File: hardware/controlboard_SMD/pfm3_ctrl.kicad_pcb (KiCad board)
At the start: 2 copper layers, 135.9 x 87 mm, 55 parts, among them J1 pfm3ControlBoard, J2 Ext, J3 0 ohm, SW1 Push, SW10 Push, SW11 Push, SW12 Push, SW2 Push, SW3 Push, SW4 Push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

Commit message: Control board v1.1
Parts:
- Enc1: value Encoder -> a
- Enc2: value Encoder -> b
- Enc3: value Encoder -> c
- Enc4: value Encoder -> d
- Enc5: value Encoder -> e
- Enc6: value Encoder -> f
- moved Enc2 46.1 mm to (151.6, 47.6)
- moved Enc5 45.7 mm to (151.6, 74.3)
- moved Enc3 37.1 mm to (188.7, 47.6)
- moved Enc4 37.0 mm to (114.6, 75.1)
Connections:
- Enc2 pad A: /h165_19 -> /H165_16
- Enc2 pad B: /h165_20 -> /H165_15
- Enc3 pad A: /H165_16 -> /H165_10
- Enc3 pad B: /H165_15 -> /H165_9
- Enc4 pad A: /H165_13 -> /h165_19
- Enc4 pad B: /H165_14 -> /h165_20
- Enc5 pad A: /H165_10 -> /H165_13
- Enc5 pad B: /H165_9 -> /H165_14
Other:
- board text added: "-"
- board text added: "Led Jmp"
- board text added: "Seq"
- board text added: "preenfm3 control v1.1 SMD Xavier Hosxe 11/2020"
- board text removed: "Led"
- board text removed: "preenfm3 control v1.1 SMD Xavier Hosxe 06/2020"

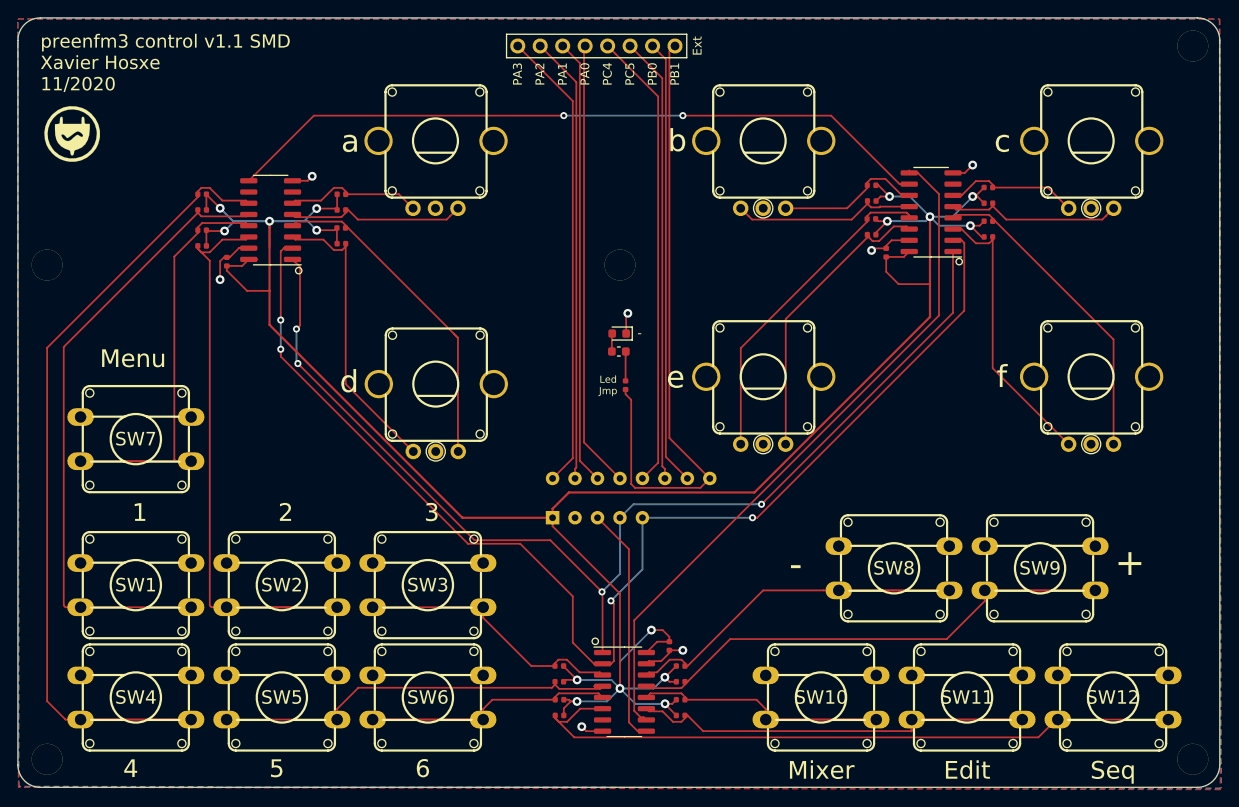
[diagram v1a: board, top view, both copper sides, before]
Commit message: PCB 1.3 : encoder 2 moved 1mm
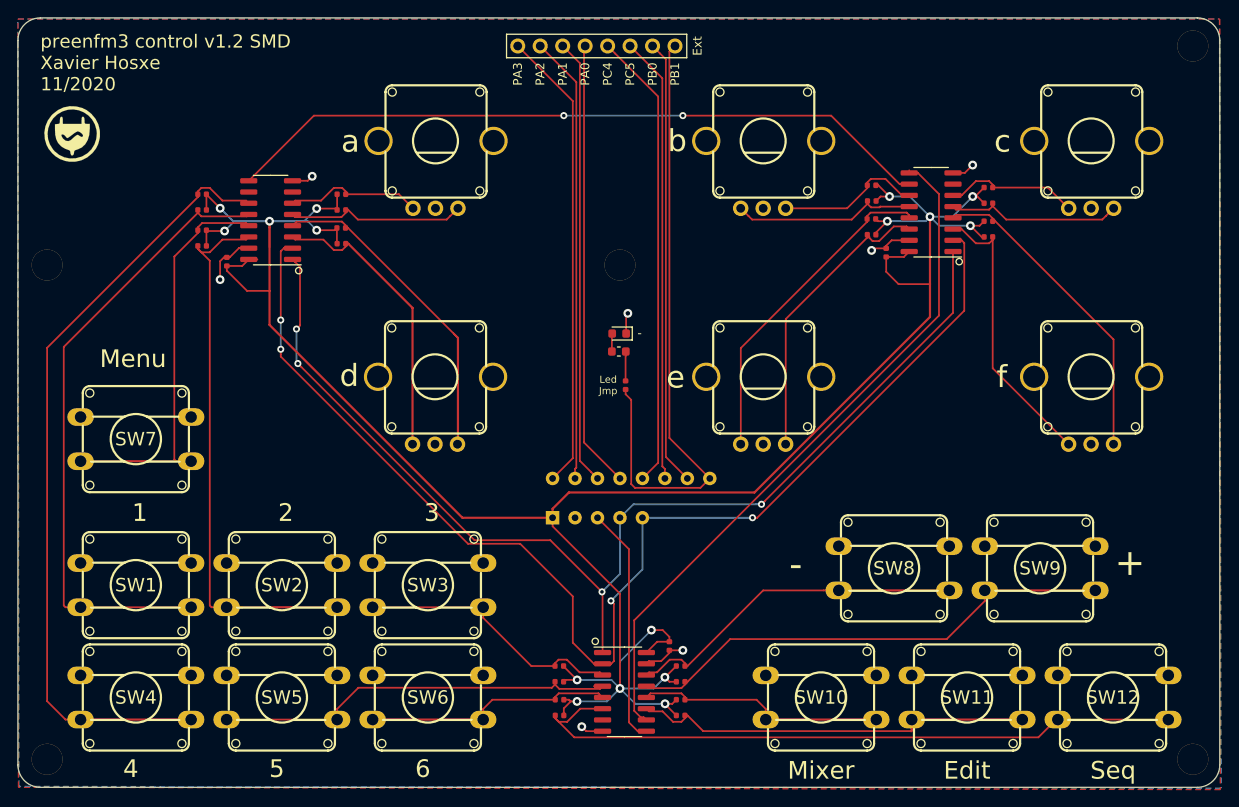
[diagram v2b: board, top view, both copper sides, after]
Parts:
- moved Enc4 0.83 mm to (114.5, 74.3)
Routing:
- net /h165_19: track 38.0 -> 37.3 mm
- net /h165_20: track 33.7 -> 33.1 mm
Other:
- board text added: "preenfm3 control v1.2 SMD Xavier Hosxe 11/2020"
- board text removed: "preenfm3 control v1.1 SMD Xavier Hosxe 11/2020"

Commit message: PCB controlboard 1.2 proto
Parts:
- removed J3: 0 ohm, Resistor_SMD:R_0402_1005Metric
- added C4: 100nF, Capacitor_SMD:C_0402_1005Metric, F.Cu at (89.6, 57.1)
- added J4: ExtButton, Connector_PinSocket_2.54mm:PinSocket_1x03_P2.54mm_Vertical, F.Cu at (95.1, 37.5)
- added R26: 10k, Resistor_SMD:R_0402_1005Metric, F.Cu at (87.0, 49.1)
- added R27: 10k, Resistor_SMD:R_0402_1005Metric, F.Cu at (87.0, 51.0)
- added R28: 10k, Resistor_SMD:R_0402_1005Metric, F.Cu at (87.0, 53.0)
- added R29: 10k, Resistor_SMD:R_0402_1005Metric, F.Cu at (87.0, 55.0)
- added R30: 10k, Resistor_SMD:R_0402_1005Metric, F.Cu at (100.8, 55.0)
- added R31: 10k, Resistor_SMD:R_0402_1005Metric, F.Cu at (100.8, 53.1)
- added R32: 10k, Resistor_SMD:R_0402_1005Metric, F.Cu at (100.8, 51.1)
- added R33: 10k, Resistor_SMD:R_0402_1005Metric, F.Cu at (100.8, 49.0)
- added U4: 74hc165, Package_SO:SOIC-16_3.9x9.9mm_P1.27mm, F.Cu at (94.4, 52.0)
- J2: footprint A_PFM3:CtrlBoard_exp_1x08 -> Connector_PinSocket_2.54mm:PinSocket_1x10_P2.54mm_Vertical
- moved R2 7.66 mm to (86.6, 61.1)
- moved R3 7.66 mm to (86.6, 62.9)
- moved R5 7.66 mm to (86.6, 66.9)
- moved R7 7.66 mm to (102.3, 64.9)
- moved R8 7.66 mm to (102.3, 62.9)
- moved R9 7.66 mm to (102.3, 61.1)
- moved C3 7.66 mm to (89.3, 68.7)
- moved R4 7.66 mm to (86.6, 65.2)
- moved U1 7.66 mm to (94.3, 64.0)
- moved R6 7.66 mm to (102.3, 66.7)
- moved L1 3.12 mm to (73.6, 49.8)
- moved J2 2.75 mm to (121.2, 37.7)
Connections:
- J2 pad 1: Net-(J1-Pad6) -> VCC
- J2 pad 2: Net-(J1-Pad7) -> GND
- J2 pad 3: Net-(J1-Pad8) -> Net-(J1-Pad6)
- J2 pad 4: Net-(J1-Pad9) -> Net-(J1-Pad7)
- J2 pad 5: Net-(J1-Pad10) -> Net-(J1-Pad8)
- J2 pad 6: Net-(J1-Pad11) -> Net-(J1-Pad9)
- J2 pad 7: Net-(J1-Pad12) -> Net-(J1-Pad10)
- J2 pad 8: /LED -> Net-(J1-Pad11)
- R1 pad 1: Net-(J3-Pad2) -> /LED
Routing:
- net /EncBut6: track 0.00 -> 157.0 mm
- net /EncBut3: track 0.00 -> 119.4 mm
- net VCC: track 287.8 -> 387.1 mm, vias 16 -> 21
- net /EncBut5: track 0.00 -> 95.3 mm
- net /EncBut2: track 0.00 -> 79.9 mm
- net /EncBut1: track 0.00 -> 34.9 mm
- net Net-(U1-Pad10): track 0.00 -> 27.2 mm, vias 0 -> 2
- net /EncBut4: track 0.00 -> 25.5 mm, vias 0 -> 2
- net Net-(J4-Pad3): track 0.00 -> 19.5 mm, vias 0 -> 1
- net Net-(J4-Pad2): track 0.00 -> 18.7 mm, vias 0 -> 1
- net /h165_clk: track 141.6 -> 151.8 mm
- net /h165_load: track 127.7 -> 136.0 mm, vias 4 -> 5
- net /h165_22: track 47.9 -> 40.1 mm
- net /h165_19: track 37.3 -> 29.8 mm
- net GND: track 25.7 -> 32.6 mm, vias 7 -> 9
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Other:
- board text added: "Gnd"
- board text added: "Vcc"
- board text removed: "Led Jmp"
